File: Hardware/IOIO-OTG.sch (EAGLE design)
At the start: 53 parts, among them Q1 IRLML2244, Q2 2N7002PW, U1 PIC24FJ256GB206, U14 SWITCH_SPDT, U2 TPS62133RGTT, U3 VREG_MIC5216

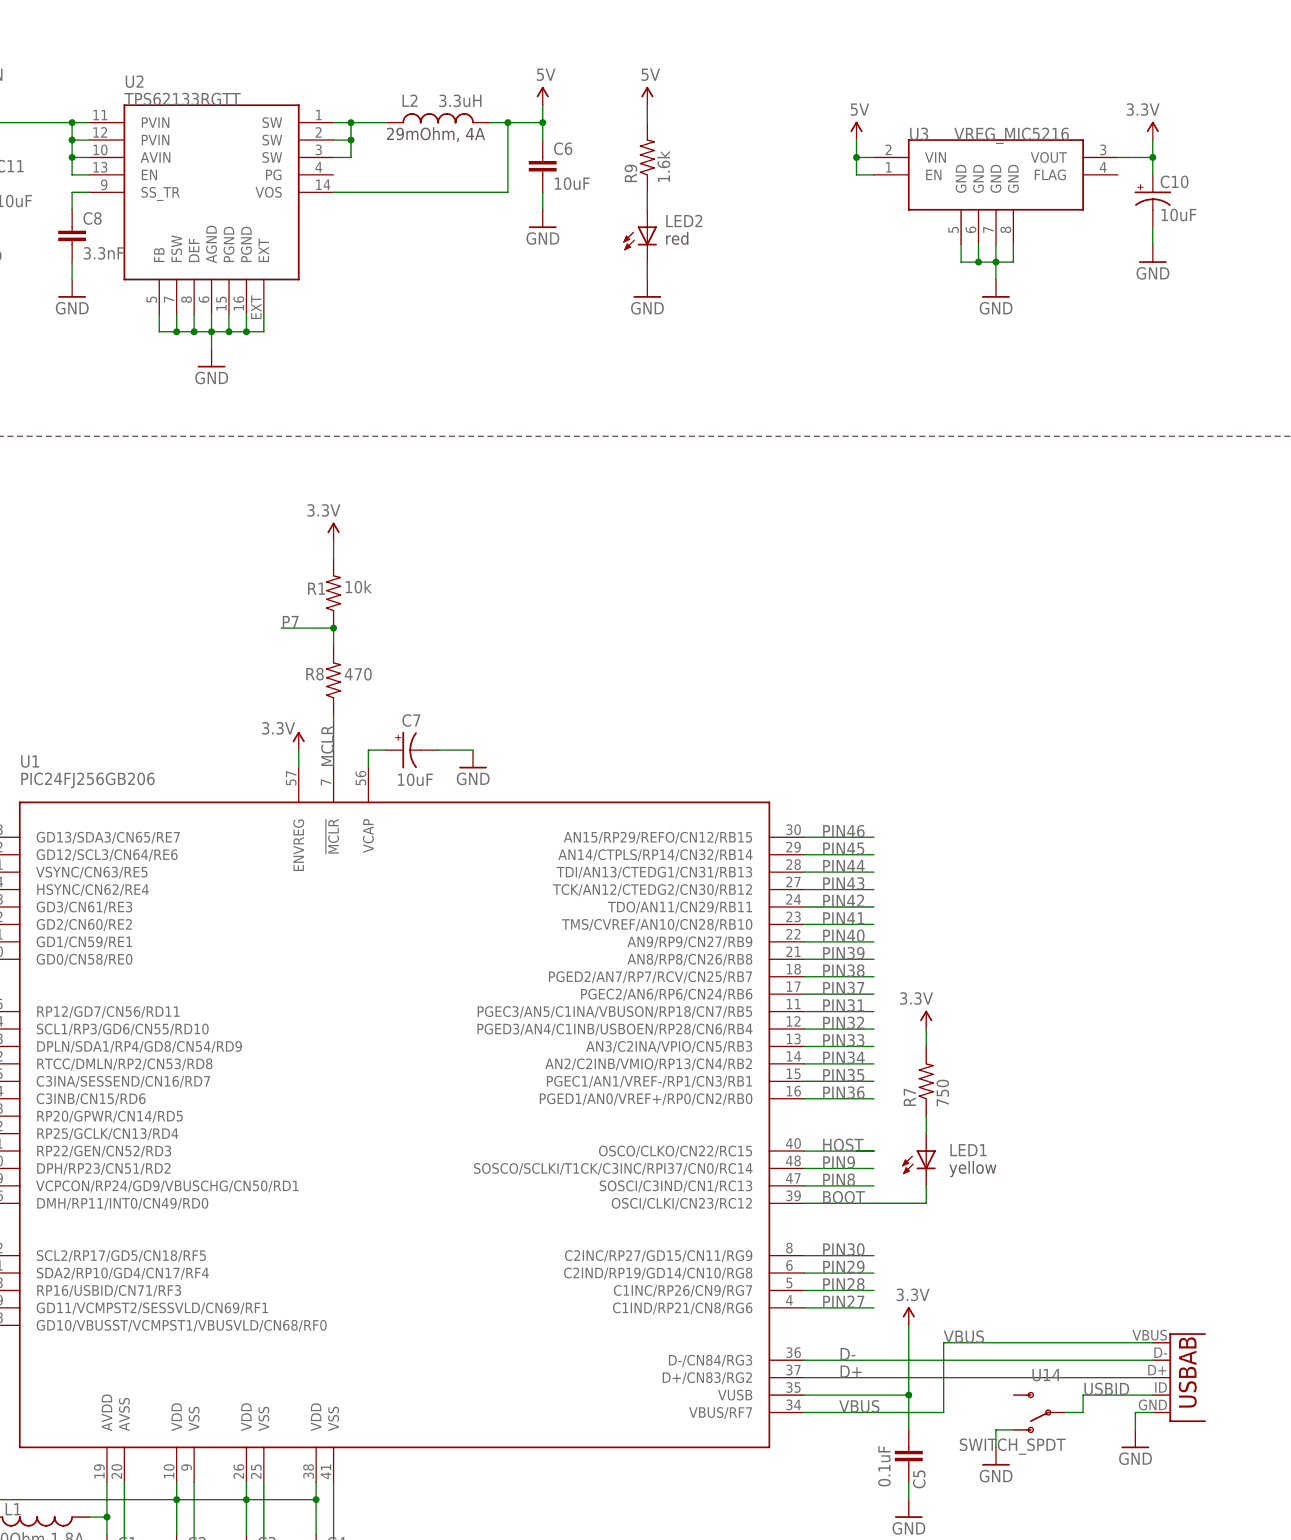
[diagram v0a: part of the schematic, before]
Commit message: Heavy Revision
(1) Created and added a new 1:1 FP for the TPS... IC
(2) Routed all traces directly out from the TPS... IC
(3) 0402 --> 0603
(4) Created and added a new FP for a new microAB USB connector, this new
FP is based off of the data-sheet for the new USB microAB that should
have guiding bosses (very much trial right now).
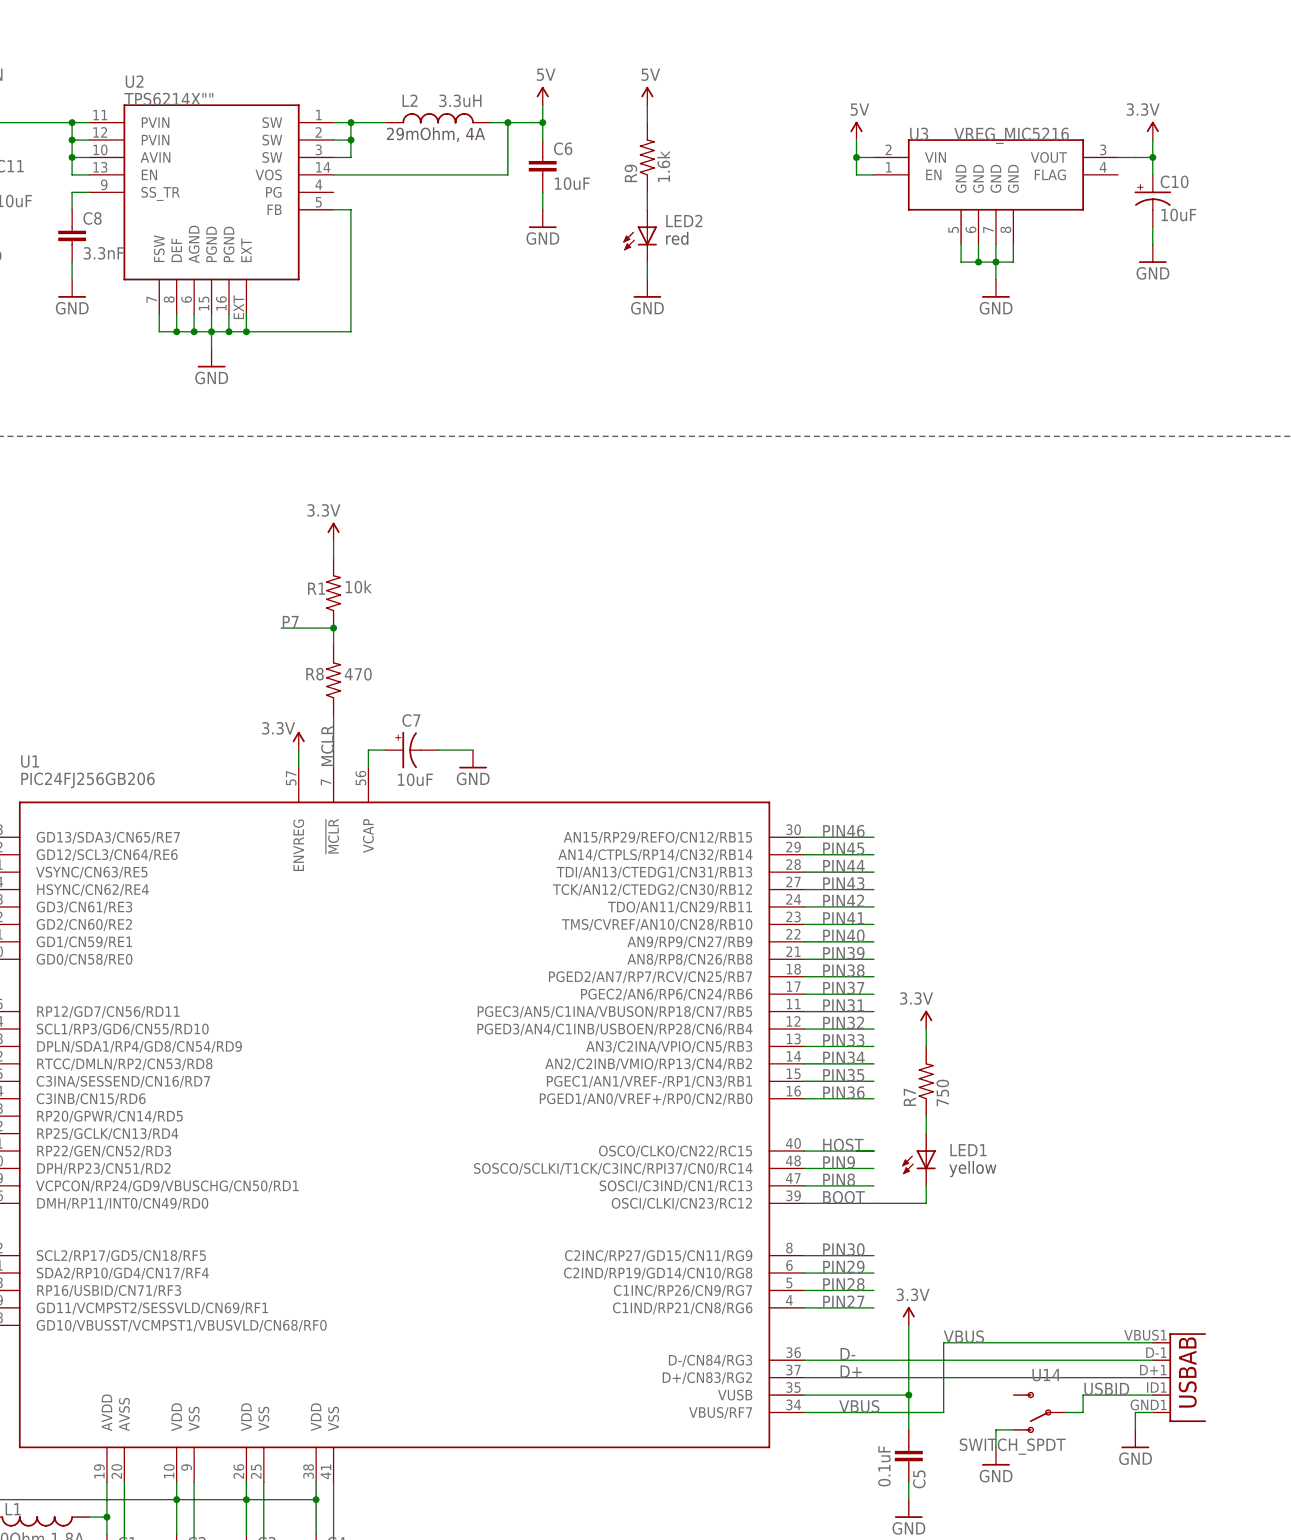
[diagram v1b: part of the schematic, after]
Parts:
- removed U$3: 10104111-0001LF, SparkFun-Connectors:USB_AB
- added U4: (no value), Testing:USB-AB""
- C1, C2, C3, C4, C5, C8: device SparkFun:CAP0402-CAP -> SparkFun-Capacitors:CAP0603-CAP
- L1: device SparkFun-Passives:INDUCTOR0402 -> SparkFun-Passives:INDUCTOR0603
- LED1: device SparkFun:LED0603 -> SparkFun-LED:LED0603
- R1, R2, R7, R8, R9: device SparkFun:RESISTOR0402-RES -> SparkFun-Resistors:RESISTOR0603-RES
- U2: value TPS62133RGTT -> TPS6214X""; device SparkFun-PowerIC:TPS6214X -> SparkFun-PowerIC:TPS6214X""
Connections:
- net D+: now also U4.D+; no longer U$3.D+
- net D-: now also U4.D-; no longer U$3.D-
- net GND: now also U4.GND; no longer U$3.GND
- net USBID: now also U4.USBID; no longer U$3.USBID
- net VBUS: now also U4.VBUS; no longer U$3.VBUS
